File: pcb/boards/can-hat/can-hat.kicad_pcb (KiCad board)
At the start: 2 copper layers, 65 x 56 mm, 30 parts, among them J1 Raspberry_Pi_GPIO, J2 OBD-II, J3 CAN_Term, J4 Audio, U1 AMS1117-3.3, U2 MCP2515, U3 SN65HVD230, Y1 16MHz

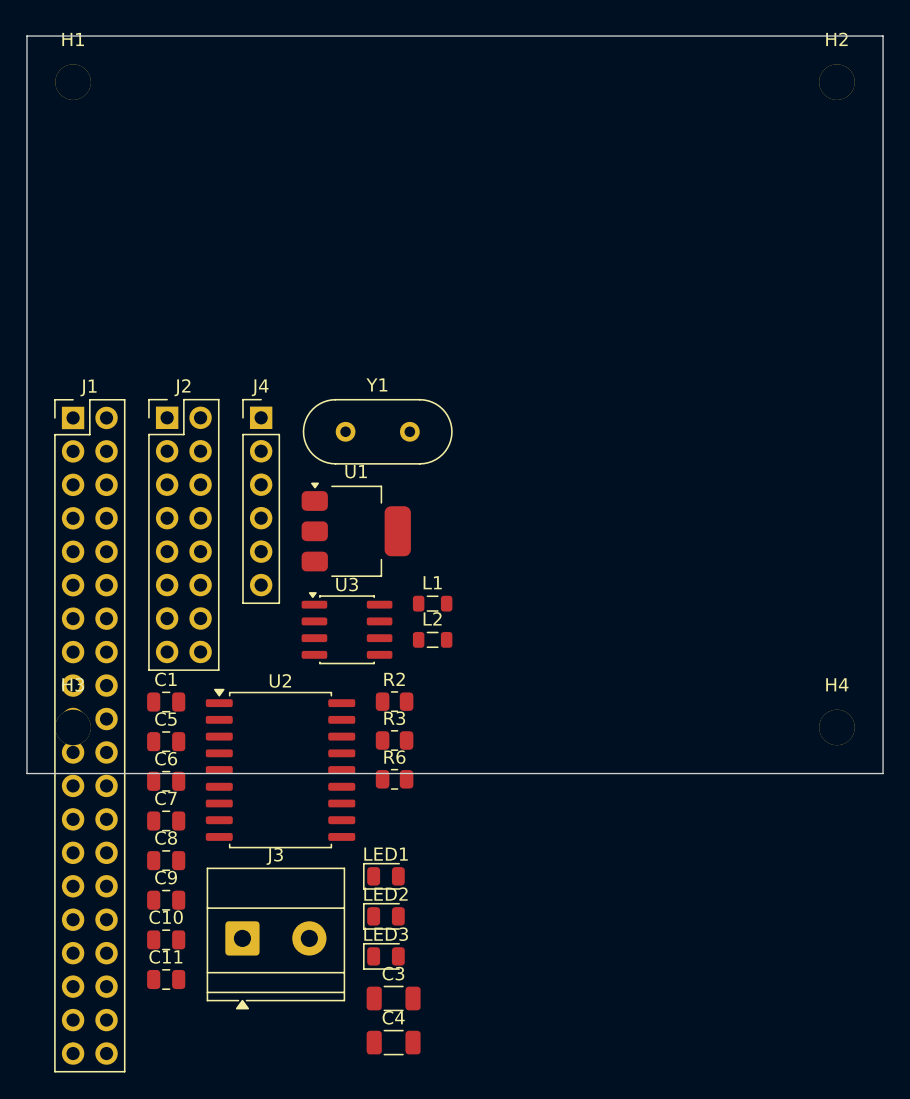
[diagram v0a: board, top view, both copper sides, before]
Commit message: CAN HAT PCB: Complete routing via FreeRouting with ground pour
- SMD components (caps, resistors, ferrites) moved to back layer
- GPIO header J1 pads flipped to correct pin orientation
- Auto-routed via FreeRouting, manual fix for CANL trace
- B.Cu ground pour with thermal reliefs
- DRC: 61 warnings (all cosmetic - mounting holes, text orientation)
- 0 unconnected pads, board ready for manufacturing

Co-Authored-By: Claude Opus 4.5 <noreply@anthropic.com>
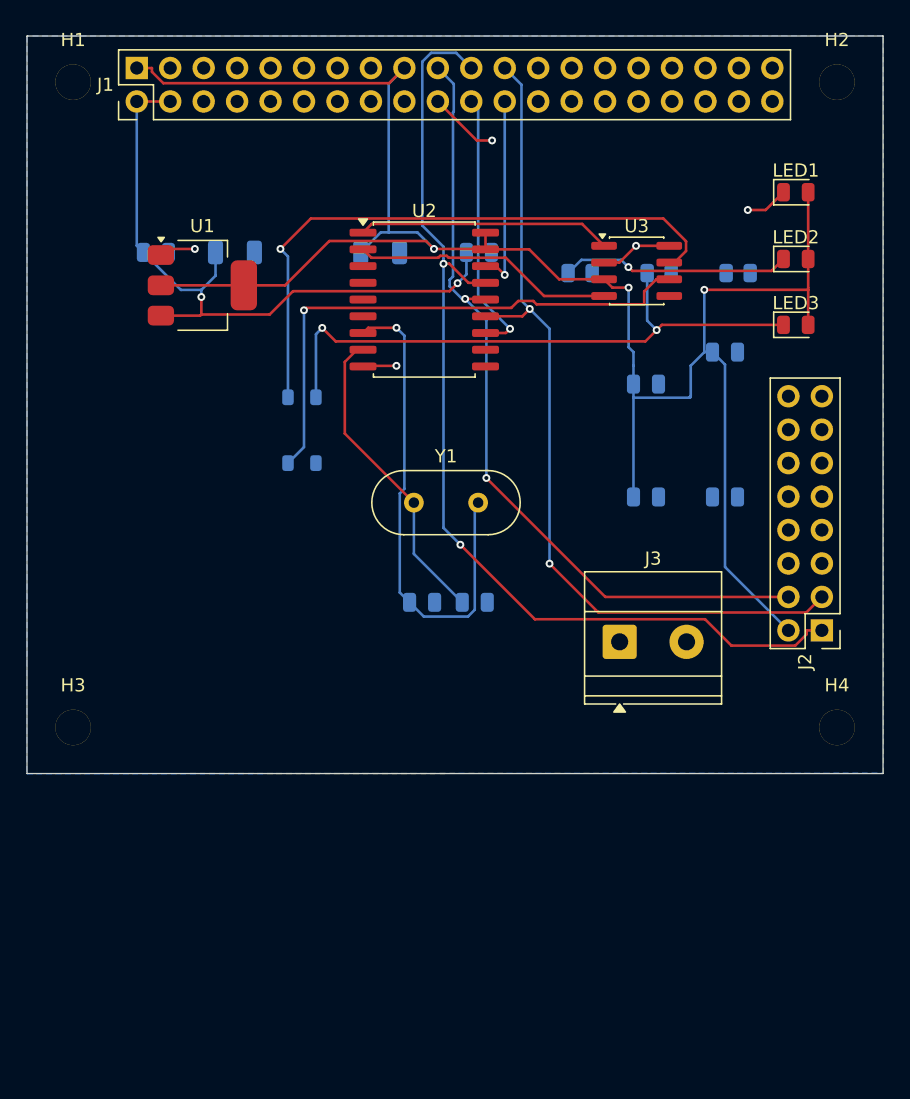
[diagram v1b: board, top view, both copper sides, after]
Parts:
- removed J4: Audio, Connector_PinHeader_2.54mm:PinHeader_1x06_P2.54mm_Vertical
- C1, C10, C11, C3, C4, C5, C6, C7, C8, C9, L1, L2, R2, R3, R6: moved to B.Cu
- moved LED1 60.6 mm to (173.1, 44.4)
- moved C4 60.0 mm to (141.5, 49.0)
- moved C9 59.4 mm to (167.7, 56.6)
- moved LED2 58.8 mm to (173.1, 49.5)
- moved C3 57.9 mm to (130.5, 49.0)
- moved LED3 57.2 mm to (173.1, 54.5)
- moved C11 56.1 mm to (167.7, 67.6)
- moved J2 52.3 mm to (175.0, 77.7), turned to 180 degrees
- moved C8 51.3 mm to (161.7, 59.0)
- moved C10 49.6 mm to (161.7, 67.6)
- moved C7 49.3 mm to (149.0, 49.0)
- moved R6 46.5 mm to (168.7, 50.6)
- moved R3 40.8 mm to (162.7, 50.6)
- moved U2 37.4 mm to (144.8, 52.6)
- moved J3 36.4 mm to (159.7, 78.6)
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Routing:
- net +3.3V: track 0.00 -> 151.9 mm, vias 0 -> 3
- net SPI_MISO: track 0.00 -> 77.8 mm, vias 0 -> 2
- net SPI_SCLK: track 0.00 -> 65.3 mm, vias 0 -> 2
- net SPI_MOSI: track 0.00 -> 61.3 mm, vias 0 -> 2
- net +5V: track 0.00 -> 51.1 mm, vias 0 -> 2
- net /CANH_U5: track 0.00 -> 46.4 mm, vias 0 -> 1
- net CANH: track 0.00 -> 46.1 mm, vias 0 -> 2
- net /CANL_U5: track 0.00 -> 41.6 mm, vias 0 -> 1
- net /OSC2: track 0.00 -> 38.1 mm, vias 0 -> 1
- net /OSC1: track 0.00 -> 23.7 mm
- net CAN_INT: track 0.00 -> 20.5 mm, vias 0 -> 1
- net CAN_RX: track 0.00 -> 19.9 mm
- net GND: track 0.00 -> 19.6 mm, vias 0 -> 5
- net CAN_TX: track 0.00 -> 19.3 mm
- net Net-(LED2-K): track 0.00 -> 17.5 mm, vias 0 -> 1
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- added copper zone on B.Cu, net GND
